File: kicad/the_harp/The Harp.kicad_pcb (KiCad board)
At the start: 4 copper layers, 56 x 94.5 mm, 28 parts, among them J401 PJ-063AH, J402 NMJ6HCD2, J403 NMJ6HCD2, J404 NMJ6HCD2, J405 Footswitch, J406 NMJ6HCD2, K401 G6K-2F-Y, Q401 2N7002, Q402 2N7002, SW101 SPDT, SW102 SPDT, SW103 SPDT

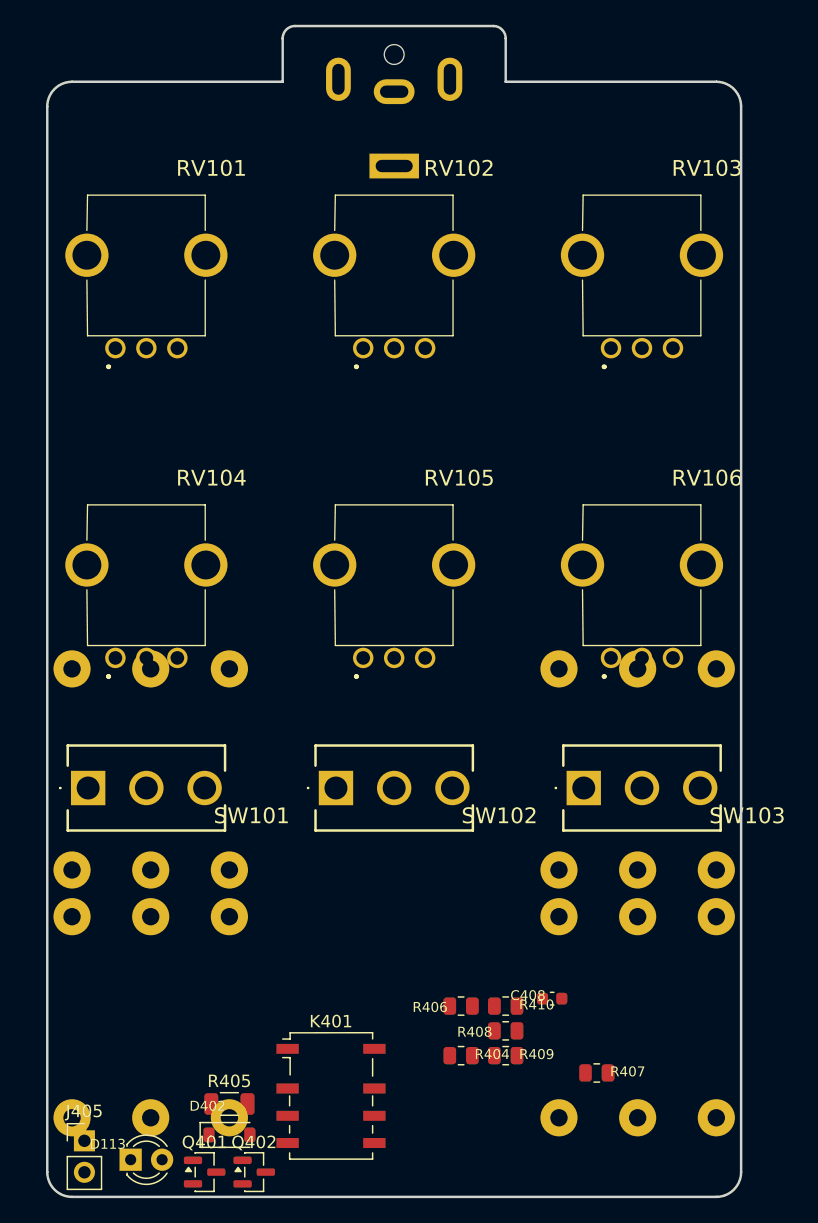
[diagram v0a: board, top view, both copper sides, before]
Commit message: Face as The Alchemist's: four knobs, three ON-ON-ON toggles
The Relic's six knobs and three toggles did not fit the four jacks: the
outer lower-row pots' pins sat on the upper jacks' rear pads and the outer
toggles over the jack bodies.

- Knobs: Mix, Sustain, Strings (row +38), Jawari (0, +13); RV104/RV106
  removed. Pots on PA0, PA1, PA2, PA4.
- Toggles: Taiway 100-DP6-T200B1M2QE ON-ON-ON (The Alchemist's part),
  Tuning Follow/Key/Drone and Brightness Dark/Warm/Glassy at (+-20, +13),
  Retune Snap/Glide/Lock at (0, -5); two MCU inputs each (PE11-PE15, PB10).
- PCB: toggles on the Alchemist footprint, RV104/RV106 deleted, bypass
  footswitch on R2816 pads, R405/D402 moved off J403's rear pads. No
  through-hole pad over a jack.
- Docs and design report: decision 13, face schedule, pin map, firmware
  requirements (TUN-11 Lock, TGL-1..3, bypass mode and expression target in
  the secondary layer).

Co-Authored-By: Claude Opus 5.5 <noreply@anthropic.com>
Claude-Session: https://claude.ai/code/session_01ToUUHuo6mg178NkLtQkDLg
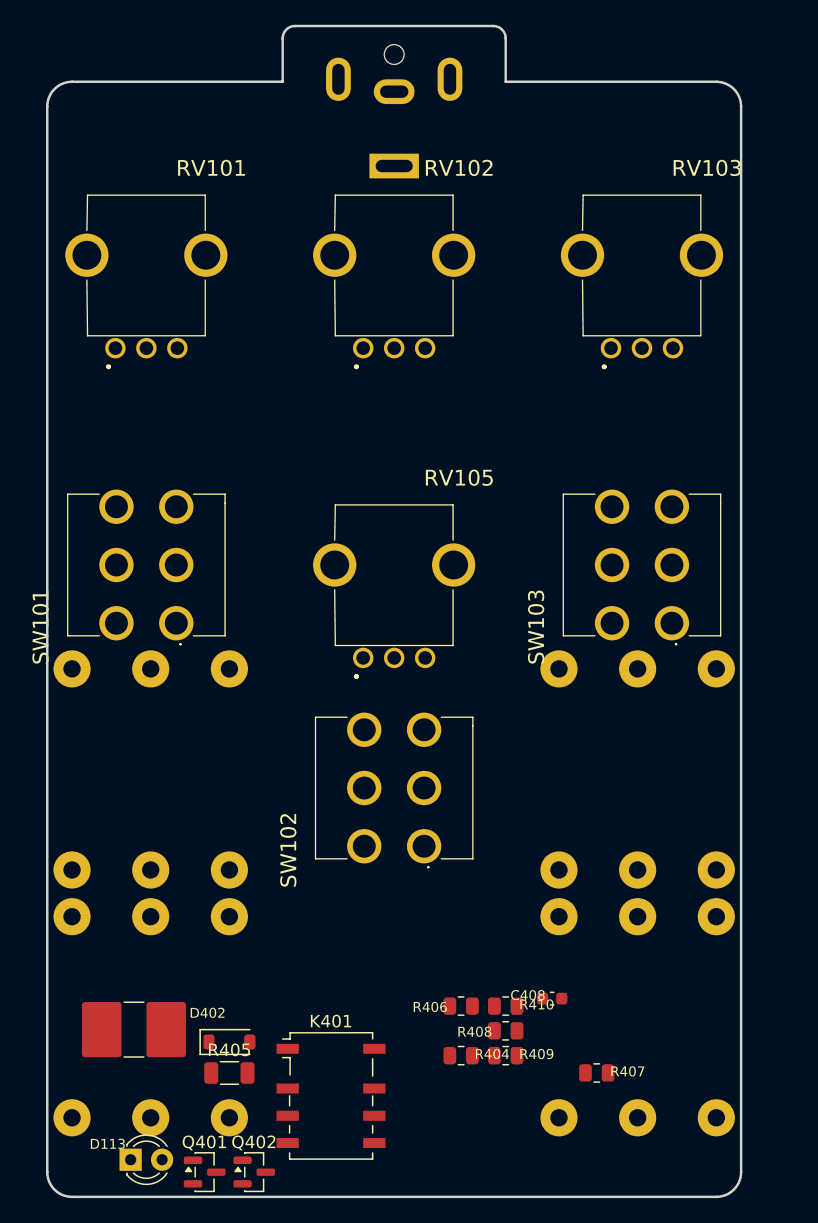
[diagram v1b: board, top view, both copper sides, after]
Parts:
- removed RV104: A100K, Potentiometer_THT:RD901F4015R1B10K00DL1
- removed RV106: B10K, Potentiometer_THT:RD901F4015R1B10K00DL1
- J405: value Footswitch -> Bypass FSW; footprint Connector_PinHeader_2.54mm:PinHeader_1x02_P2.54mm_Vertical -> Resistor_SMD:R_2816_7142Metric_Pad3.20x4.45mm_HandSolder
- SW101, SW102, SW103: value SPDT -> 100-DP6; footprint SPDT Switches:SPDT love my Switches -> SPDT Switches:100DP3T1B2M2QE
- moved SW101 15.1 mm to (130.9, 96.7)
- moved SW103 15.1 mm to (170.9, 96.7)
- moved J405 9.83 mm to (127.5, 129.5)
- moved SW102 8.53 mm to (150.9, 114.7)
- moved D402 7.50 mm to (135.2, 130.5)
- moved R405 2.50 mm to (135.2, 133.0)
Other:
- board text added: "BRIGHTNESS SW103"
- board text added: "MIX RV101"
- board text added: "RETUNE SW102"
- board text added: "TUNING SW101"
- board text removed: "BRIGHTNESS RV104"
- board text removed: "BYPASS MODE SW102"
- board text removed: "EXP TARGET SW103"
- board text removed: "MIX RV106"
- board text removed: "SNAP/GLIDE SW101"
- board text removed: "TUNING RV101"
